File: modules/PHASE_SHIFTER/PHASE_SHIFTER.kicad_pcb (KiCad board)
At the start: 2 copper layers, 160 x 100 mm, 79 parts, among them IC1 LM324, IC2 LM324, IC3 OpAmp, IC4 OpAmp, J1 Card_Connector, J2 MonoJack, J3 OS, J4 +, J5 -, J6 0, J7 IS SELECT, J8 OS SELECT, P1 470k, P2 50k, P3 10k, P4 10k, P5 50k, T1 N-FET, T2 N-FET, T3 N-FET, T4 N-FET, T5 N-FET, T6 N-FET

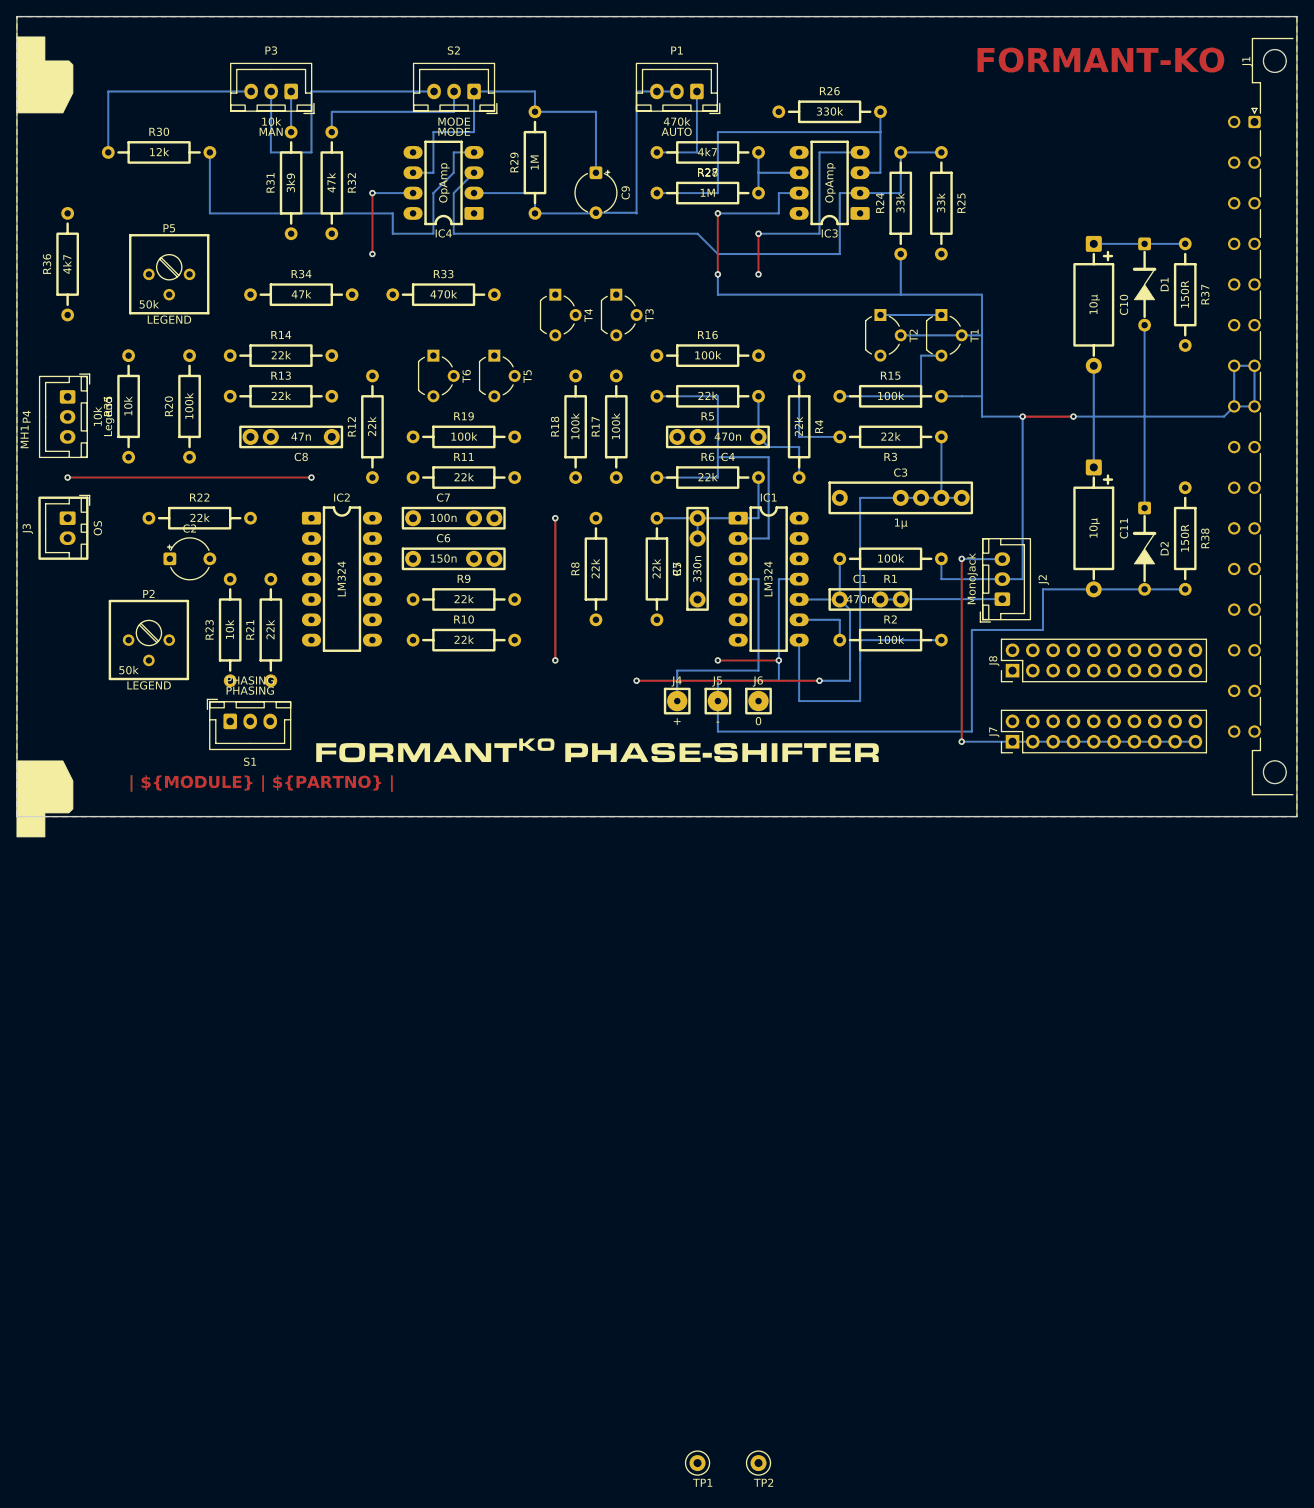
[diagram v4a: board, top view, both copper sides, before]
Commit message: phase shifter module ready for proto
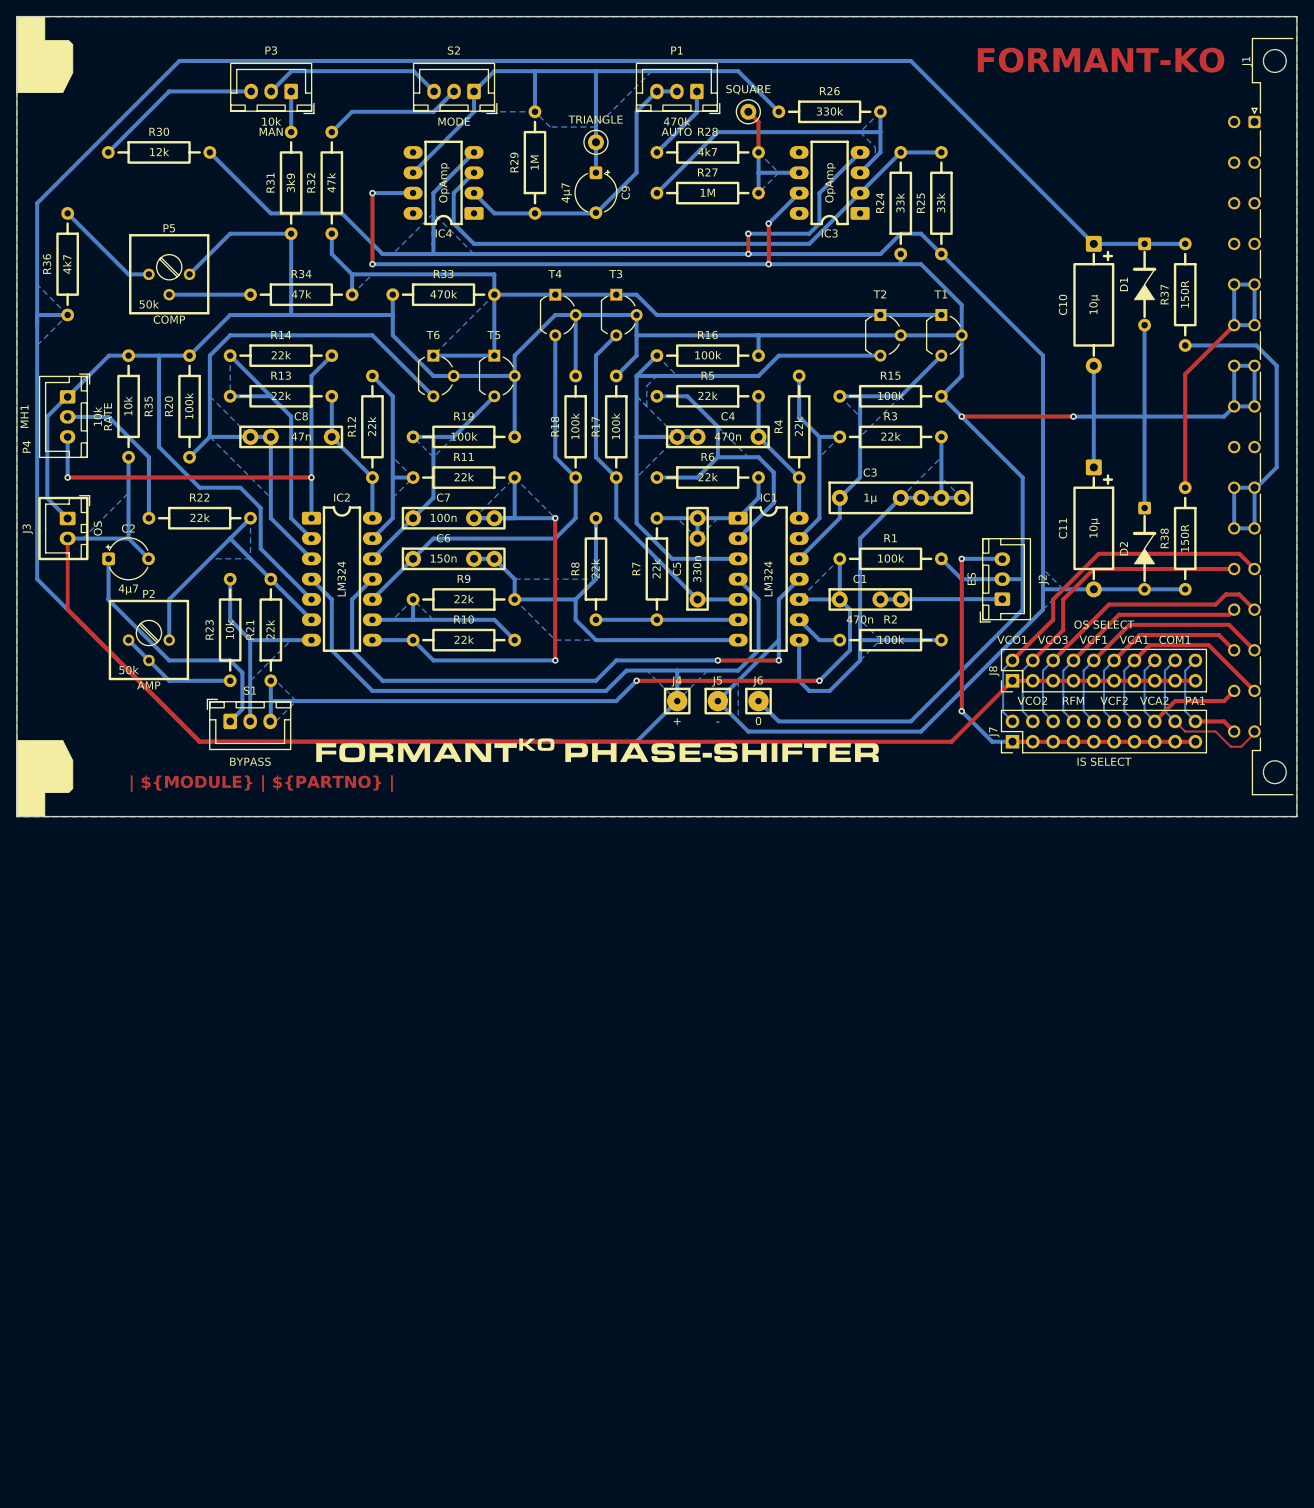
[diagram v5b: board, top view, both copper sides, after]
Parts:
- J2: value MonoJack -> ES
- S1: value PHASING -> BYPASS
- moved TP1 169.0 mm to (146.4, 56.9)
- moved TP2 166.3 mm to (127.4, 60.7)
- moved C2 7.66 mm to (66.5, 112.8)
- moved MH1 2.54 mm to (55.0, 95.0)
- moved J8 1.27 mm to (179.4, 128.0)
- turned R10 to 180 degrees
- turned R11 to 180 degrees
- turned R12 to -90 degrees
- turned R13 to 180 degrees
- turned R16 to 180 degrees
- turned R17 to -90 degrees
- turned R18 to -90 degrees
- turned R19 to 180 degrees
- turned R20 to -90 degrees
- turned R23 to -90 degrees
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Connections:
- C6 pad 1: Net-(C6-Pad1) -> Net-(IC2C-+)
- C6 pad 2: Net-(IC2C-+) -> Net-(C6-Pad2)
- C7 pad 1: Net-(C7-Pad1) -> Net-(IC2D-+)
- C7 pad 2: Net-(IC2D-+) -> Net-(C7-Pad2)
- IC1 pad 7: Net-(C6-Pad1) -> Net-(C6-Pad2)
- IC2 pad 7: Net-(S1-a) -> Net-(S1-b)
- IC2 pad 8: Net-(C7-Pad1) -> Net-(C7-Pad2)
- R10 pad 2: Net-(C7-Pad1) -> Net-(C7-Pad2)
- R11 pad 1: Net-(C7-Pad1) -> Net-(C7-Pad2)
- R23 pad 1: Net-(S1-a) -> Net-(S1-b)
- R8 pad 2: Net-(C6-Pad1) -> Net-(C6-Pad2)
- R9 pad 1: Net-(C6-Pad1) -> Net-(C6-Pad2)
- S1 pad 1: Net-(S1-a) -> Net-(IC1C-+)
- S1 pad 3: Net-(IC1C-+) -> Net-(S1-b)
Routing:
- net +12V: track 39.4 -> 384.2 mm
- net GND: track 250.5 -> 519.3 mm, vias 8 -> 6
- net OS: track 0.00 -> 181.2 mm
- net -12V: track 192.8 -> 340.5 mm
- net Net-(T1-G): track 7.62 -> 101.2 mm
- net Net-(IC1A-+): track 0.00 -> 75.7 mm
- net Net-(IC2A-+): track 0.00 -> 70.9 mm
- net Net-(C7-Pad2): track 0.00 -> 60.7 mm, vias 0 -> 2
- net Net-(IC2-Pad1): track 0.00 -> 56.9 mm, vias 0 -> 2
- net Net-(IC2C-+): track 0.00 -> 53.5 mm
- net Net-(C6-Pad2): track 0.00 -> 51.4 mm
- net Net-(IC1C-+): track 47.5 -> 97.1 mm
- net VCO1: track 0.00 -> 46.6 mm
- net Net-(IC1B-+): track 0.00 -> 44.4 mm
- net +15V: track 0.00 -> 44.2 mm
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- added copper zone on B.Cu, net +12V
- added copper zone on B.Cu, net +15V
- added copper zone on B.Cu, net -12V
- added copper zone on B.Cu, net -15V
- added copper zone on B.Cu, net Net-(C3-Pad2)
- added copper zone on B.Cu, net Net-(C5-Pad2)
- added copper zone on B.Cu, net Net-(C6-Pad2)
- added copper zone on B.Cu, net Net-(C7-Pad2)
- added copper zone on B.Cu, net Net-(IC1A-+)
- added copper zone on B.Cu, net Net-(IC1A--)
- added copper zone on B.Cu, net Net-(IC1C-+)
- added copper zone on B.Cu, net Net-(IC1D-+)
- added copper zone on B.Cu, net Net-(IC1D--)
- added copper zone on B.Cu, net Net-(IC2A-+)
- added copper zone on B.Cu, net Net-(IC2A--)
- added copper zone on B.Cu, net Net-(IC2B--)
- added copper zone on B.Cu, net Net-(IC2C--)
- added copper zone on B.Cu, net Net-(IC2D-+)
- added copper zone on B.Cu, net Net-(IC2D--)
- added copper zone on B.Cu, net Net-(IC3-+)
- added copper zone on B.Cu, net Net-(IC3-Pad6)
- added copper zone on B.Cu, net Net-(S1-b)
- added copper zone on B.Cu, net Net-(S2-a)
- added copper zone on B.Cu, net Net-(T1-G)
- added copper zone on B.Cu, net OS
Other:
- board text added: "COM1"
- board text added: "PA1"
- board text added: "RFM"
- board text added: "VCA1"
- board text added: "VCA2"
- board text added: "VCF1"
- board text added: "VCF2"
- board text added: "VCO1"
- board text added: "VCO2"
- board text added: "VCO3"
